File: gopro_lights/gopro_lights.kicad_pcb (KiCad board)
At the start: 2 copper layers, 64.2 x 58.6 mm, 8 parts, among them J1 Screw_Terminal_01x02

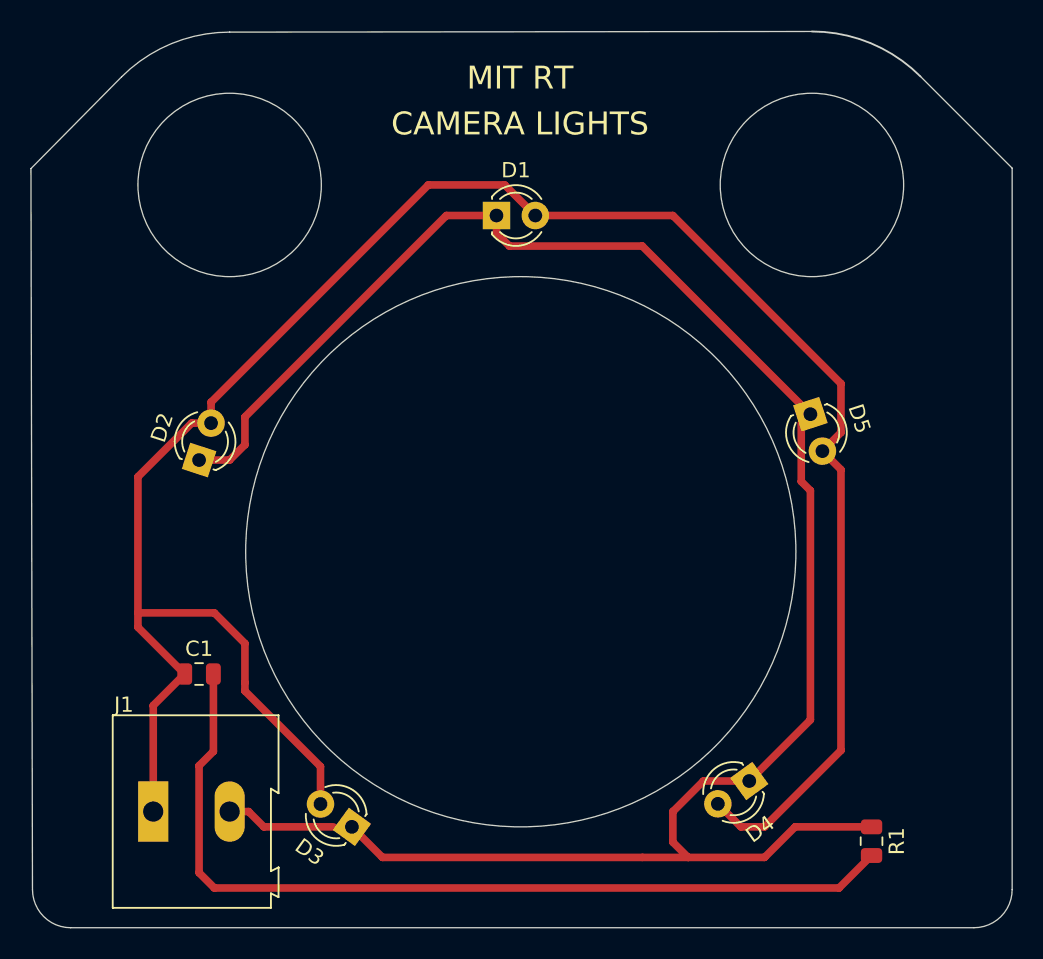
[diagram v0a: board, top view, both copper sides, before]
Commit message: fix: for hole size
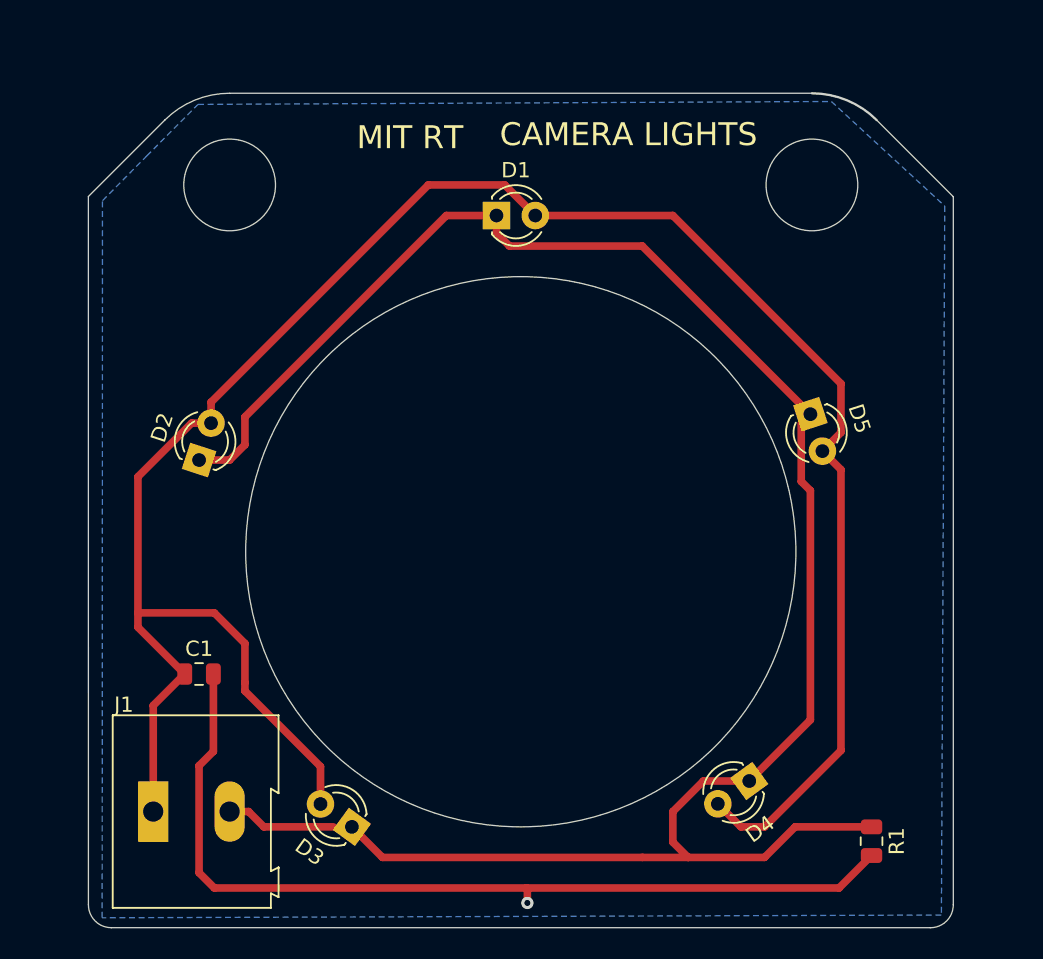
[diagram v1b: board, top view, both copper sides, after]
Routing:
- net GND: track 58.7 -> 59.7 mm, vias 0 -> 1
- added copper zone on B.Cu, net GND
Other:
- board size 64.2 x 58.6 mm -> 56.6 x 54.6 mm
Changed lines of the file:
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@@
   (general
     (thickness 1.6)
-    (drawings 21)
-    (tracks 60)
+    (drawings 18)
+    (tracks 64)
     (zones 0)
     (modules 8)
@@
   )
   (page A4)
+  (title_block
+    (title "MIT Rocket Team Hermes 3 Go Pro Lights")
+    (date 2019-11-18)
+    (rev 1)
+    (company "MIT RT")
+    (comment 1 "Jacob Miske")
+  )
   (layers
     (0 F.Cu signal)
@@
       (effects (font (size 1 1) (thickness 0.15)))
     )
-    (fp_text value Screw_Terminal_01x02 (at 5 6) (layer F.Fab)
+    (fp_text value Screw_Terminal_01x02 (at 4.83 6.33) (layer F.Fab)
       (effects (font (size 1 1) (thickness 0.15)))
     )
@@
     )
   )
-  (dimension 64.200007 (width 0.15) (layer Dwgs.User)
-    (gr_text "64.200 mm" (at 106.092189 46.19907 0.0267737268) (layer Dwgs.User)
-      (effects (font (size 1 1) (thickness 0.15)))
-    )
-    (feature1 (pts (xy 138.2 62.9) (xy 138.192522 46.897649)))
-    (feature2 (pts (xy 74 62.93) (xy 73.992522 46.927649)))
-    (crossbar (pts (xy 73.992796 47.51407) (xy 138.192796 47.48407)))
-    (arrow1a (pts (xy 138.192796 47.48407) (xy 137.066566 48.071017)))
-    (arrow1b (pts (xy 138.192796 47.48407) (xy 137.066018 46.898176)))
-    (arrow2a (pts (xy 73.992796 47.51407) (xy 75.119574 48.099964)))
-    (arrow2b (pts (xy 73.992796 47.51407) (xy 75.119026 46.927123)))
-  )
+  (gr_arc (start 79.257359 111.1) (end 77.76 111.1) (angle -90) (layer Edge.Cuts) (width 0.05))
+  (gr_arc (start 132.85 111.1) (end 132.85 112.6) (angle -90) (layer Edge.Cuts) (width 0.05))
+  (gr_line (start 77.757359 64.757359) (end 77.76 111.1) (layer Edge.Cuts) (width 0.05))
+  (gr_line (start 134.35 64.77) (end 134.35 111.1) (layer Edge.Cuts) (width 0.05))
+  (gr_line (start 77.757359 64.757359) (end 82.757359 59.757359) (layer Edge.Cuts) (width 0.05))
+  (gr_line (start 129.35 59.77) (end 134.35 64.77) (layer Edge.Cuts) (width 0.05))
+  (gr_arc (start 125.1 64) (end 129.339999 59.760001) (angle -45) (layer Edge.Cuts) (width 0.15))
   (dimension 38.1 (width 0.15) (layer Dwgs.User)
     (gr_text "38.100 mm" (at 106.05 50.7) (layer Dwgs.User)
@@
     (arrow2b (pts (xy 88.05 85.2) (xy 89.176504 84.613579)))
   )
-  (dimension 12 (width 0.15) (layer Dwgs.User)
-    (gr_text "12.000 mm" (at 127.5 64 270) (layer Dwgs.User)
-      (effects (font (size 1 1) (thickness 0.15)))
-    )
-    (feature1 (pts (xy 125.1 70) (xy 126.786421 70)))
-    (feature2 (pts (xy 125.1 58) (xy 126.786421 58)))
-    (crossbar (pts (xy 126.2 58) (xy 126.2 70)))
-    (arrow1a (pts (xy 126.2 70) (xy 125.613579 68.873496)))
-    (arrow1b (pts (xy 126.2 70) (xy 126.786421 68.873496)))
-    (arrow2a (pts (xy 126.2 58) (xy 125.613579 59.126504)))
-    (arrow2b (pts (xy 126.2 58) (xy 126.786421 59.126504)))
-  )
-  (dimension 49.7 (width 0.15) (layer Dwgs.User)
-    (gr_text "49.700 mm" (at 142.5 87.75 270) (layer Dwgs.User)
-      (effects (font (size 1 1) (thickness 0.15)))
-    )
-    (feature1 (pts (xy 138.2 112.6) (xy 141.786421 112.6)))
-    (feature2 (pts (xy 138.2 62.9) (xy 141.786421 62.9)))
-    (crossbar (pts (xy 141.2 62.9) (xy 141.2 112.6)))
-    (arrow1a (pts (xy 141.2 112.6) (xy 140.613579 111.473496)))
-    (arrow1b (pts (xy 141.2 112.6) (xy 141.786421 111.473496)))
-    (arrow2a (pts (xy 141.2 62.9) (xy 140.613579 64.026504)))
-    (arrow2b (pts (xy 141.2 62.9) (xy 141.786421 64.026504)))
-  )
-  (gr_arc (start 135.7 110.1) (end 135.7 112.6) (angle -90) (layer Edge.Cuts) (width 0.05))
-  (gr_arc (start 76.6 110.1) (end 74.1 110.1) (angle -90) (layer Edge.Cuts) (width 0.05))
-  (gr_line (start 138.2 62.9) (end 138.2 110.1) (layer Edge.Cuts) (width 0.05))
-  (gr_line (start 76.6 112.6) (end 135.7 112.6) (layer Edge.Cuts) (width 0.05))
-  (gr_line (start 74 62.93) (end 74.1 110.1) (layer Edge.Cuts) (width 0.05))
-  (gr_line (start 132.199999 56.900001) (end 138.2 62.9) (layer Edge.Cuts) (width 0.05))
-  (gr_line (start 79.928932 56.928932) (end 74 62.93) (layer Edge.Cuts) (width 0.05))
-  (gr_arc (start 87 64) (end 87 54) (angle -45) (layer Edge.Cuts) (width 0.05))
-  (gr_line (start 125.1 53.959085) (end 87 54) (layer Edge.Cuts) (width 0.05))
-  (gr_arc (start 125.1 64) (end 132.199999 56.900001) (angle -45) (layer Edge.Cuts) (width 0.12))
+  (gr_line (start 79.257359 112.597359) (end 132.85 112.6) (layer Edge.Cuts) (width 0.05))
+  (gr_arc (start 87 64) (end 87 58) (angle -45) (layer Edge.Cuts) (width 0.05))
+  (gr_line (start 125.1 58) (end 87 58) (layer Edge.Cuts) (width 0.05))
   (gr_text "Made by: Jacob Miske" (at 120 110) (layer B.SilkS)
     (effects (font (size 1.5 1.5) (thickness 0.3)) (justify mirror))
   )
-  (gr_text "CAMERA LIGHTS" (at 106 60) (layer F.SilkS)
+  (gr_text "CAMERA LIGHTS" (at 113.1 60.7) (layer F.SilkS)
     (effects (font (size 1.5 1.5) (thickness 0.3)))
   )
-  (gr_text "MIT RT" (at 106 57) (layer F.SilkS)
+  (gr_text "MIT RT" (at 98.8 60.9) (layer F.SilkS)
     (effects (font (size 1.5 1.5) (thickness 0.3)))
   )
   (gr_circle (center 106.05 88) (end 124.05 88) (layer Edge.Cuts) (width 0.05))
-  (gr_circle (center 125.1 64) (end 131.1 64) (layer Edge.Cuts) (width 0.05))
-  (gr_circle (center 87 64) (end 93 64) (layer Edge.Cuts) (width 0.05))
+  (gr_circle (center 125.1 64) (end 128.1 64) (layer Edge.Cuts) (width 0.05))
+  (gr_circle (center 87 64) (end 90 64) (layer Edge.Cuts) (width 0.05))
+  (via (at 106.48 110.98) (size 0.8) (drill 0.4) (layers F.Cu B.Cu) (net 2))
   (segment (start 105 64) (end 107 66) (width 0.5) (layer F.Cu) (net 1))
   (segment (start 100 64) (end 105 64) (width 0.5) (layer F.Cu) (net 1))
@@
   (segment (start 85 109) (end 86 110) (width 0.5) (layer F.Cu) (net 2))
   (segment (start 126.875 110) (end 129 107.875) (width 0.5) (layer F.Cu) (net 2))
-  (segment (start 86 110) (end 126.875 110) (width 0.5) (layer F.Cu) (net 2))
+  (segment (start 106.48 110.04) (end 106.44 110) (width 0.5) (layer F.Cu) (net 2))
+  (segment (start 106.48 110.98) (end 106.48 110.04) (width 0.5) (layer F.Cu) (net 2))
+  (segment (start 86 110) (end 106.44 110) (width 0.5) (layer F.Cu) (net 2))
+  (segment (start 106.44 110) (end 126.875 110) (width 0.5) (layer F.Cu) (net 2))
   (segment (start 118 103) (end 116 105) (width 0.5) (layer F.Cu) (net 3))
   (segment (start 116 105) (end 116 107) (width 0.5) (layer F.Cu) (net 3))
@@
   (segment (start 88.24 105) (end 89.24 106) (width 0.5) (layer F.Cu) (net 3))
   (segment (start 87 105) (end 88.24 105) (width 0.5) (layer F.Cu) (net 3))
+  (zone (net 2) (net_name GND) (layer B.Cu) (hatch edge 0.508)
+    (connect_pads (clearance 0.508))
+    (min_thickness 0.254)
+    (fill yes (arc_segments 32) (thermal_gap 0.508) (thermal_bridge_width 0.508))
+    (polygon
+      (pts
+        (xy 81.58 62.1) (xy 84.93 58.73) (xy 126.37 58.54) (xy 133.79 65.38) (xy 133.57 111.77)
+        (xy 78.66 111.95) (xy 78.68 65.03)
+      )
+    )
+  )
 )

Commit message: chore: adding files and .step
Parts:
- J1: footprint TerminalBlock:TerminalBlock_Altech_AK300-2_P5.00mm -> TerminalBlock:TerminalBlock_bornier-2_P5.08mm
- moved J1 0.13 mm to (82.0, 104.9)
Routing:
- net +5V: track 142.5 -> 140.1 mm
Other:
- outline, holes or cut-outs redrawn
